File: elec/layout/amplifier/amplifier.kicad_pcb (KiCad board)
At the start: 2 copper layers, 40 x 40 mm, 0 parts

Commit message: building to layout
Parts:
- added C1: , lcsc:C0402, F.Cu at (66.0, 80.6)
- added C10: , lcsc:C0805, F.Cu at (157.2, 103.8)
- added C11: 4.7µF ±10% 16V X5R, lcsc:C0603, F.Cu at (151.0, 60.2)
- added C12: 100nF ±10% 16V X7R, lcsc:C0402, F.Cu at (151.0, 55.2)
- added C13: 22µF ±20% 25V X5R, lcsc:C0805, F.Cu at (170.8, 58.0)
- added C14: , lcsc:C0805, F.Cu at (170.8, 53.0)
- added C15: , lcsc:C0805, F.Cu at (170.8, 48.0)
- added C16: , lcsc:C0402, F.Cu at (170.8, 43.0)
- added C17: , lcsc:C0402, F.Cu at (170.8, 38.0)
- added C18: , lcsc:C0402, F.Cu at (170.8, 33.0)
- added C19: , lcsc:C0402, F.Cu at (156.0, 80.6)
- added C2: 1µF ±10% 25V X5R, lcsc:C0402, F.Cu at (86.0, 80.6)
- added C3: 470nF ±10% 50V X7R, lcsc:C0603, F.Cu at (113.7, 109.1)
- added C4: , lcsc:C0603, F.Cu at (110.9, 111.3)
- added C5: 680nF ±10% 50V X7R, lcsc:C0805, F.Cu at (69.1, 109.7)
- added C6: , lcsc:C0805, F.Cu at (69.1, 104.7)
- added C7: , lcsc:C0603, F.Cu at (116.5, 109.1)
- added C8: , lcsc:C0603, F.Cu at (118.8, 111.4)
- added C9: , lcsc:C0805, F.Cu at (157.2, 108.8)
- added L1: 10µH ±20% 4.5A 68mΩ, lcsc:IND-SMD_L7.3-W6.8, F.Cu at (111.6, 103.3)
- added L2: , lcsc:IND-SMD_L7.3-W6.8, F.Cu at (104.7, 103.3)
- added L3: , lcsc:IND-SMD_L7.3-W6.8, F.Cu at (118.4, 103.3)
- added L4: , lcsc:IND-SMD_L7.3-W6.8, F.Cu at (125.3, 103.3)
- added R1: 10Ω ±1% 62.5mW, lcsc:R0402, F.Cu at (110.7, 116.6)
- added R2: 10kΩ ±1% 62.5mW, lcsc:R0402, F.Cu at (76.0, 80.6)
- added R3: , lcsc:R0402, F.Cu at (96.0, 80.6)
- added R4: , lcsc:R0402, F.Cu at (126.0, 80.6)
- added R5: , lcsc:R0402, F.Cu at (166.0, 80.6)
- added U1: _Texas_Instruments_TAS5825MRHBR, lcsc:VQFN-32_L5.0-W5.0-P0.50-TL-EP, F.Cu at (114.8, 114.6)
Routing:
- net net-10: track 0.00 -> 1.32 mm
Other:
- board outline removed
- board text removed: "{{GITHASH}}"

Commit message: Layout complete
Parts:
- L1: value 10µH ±20% 4.5A 68mΩ -> (none)
- L2: value (none) -> 10µH ±20% 4.5A 68mΩ
- moved C18 103.0 mm to (108.2, 114.8), turned to -90 degrees
- moved C17 92.4 mm to (119.2, 114.7), turned to -90 degrees
- moved C14 90.8 mm to (105.0, 115.6), turned to -90 degrees
- moved C16 87.7 mm to (120.2, 114.7), turned to -90 degrees
- moved C13 86.1 mm to (106.8, 115.6), turned to -90 degrees
- moved C15 83.5 mm to (121.6, 115.4), turned to -90 degrees
- moved C12 72.7 mm to (110.6, 115.7), turned to 90 degrees
- moved C11 69.4 mm to (109.4, 115.8), turned to 90 degrees
- moved R5 64.8 mm to (113.8, 119.0), turned to -90 degrees
- moved C1 64.3 mm to (119.4, 116.4)
- moved C19 60.0 mm to (109.7, 118.8), turned to -90 degrees
- moved R2 52.5 mm to (111.8, 119.0), turned to -90 degrees
- moved C2 49.7 mm to (119.5, 117.4)
- moved R3 41.9 mm to (112.8, 119.0), turned to -90 degrees
- moved C5 39.9 mm to (109.0, 108.8), turned to -90 degrees
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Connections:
- C1 pad 1: net-7 -> net-1
- C1 pad 2: lv -> GND
- C10 pad 2: output_stage_b-net -> GND
- C11 pad 1: hv -> DVDD
- C11 pad 2: lv -> GND
- C12 pad 1: hv -> DVDD
- C12 pad 2: lv -> GND
- C13 pad 1: power_pvdd-net -> PVDD
- C13 pad 2: net -> GND
- C14 pad 1: power_pvdd-net -> PVDD
- C14 pad 2: net -> GND
- C15 pad 1: power_pvdd-net -> PVDD
- C15 pad 2: net -> GND
- C16 pad 1: power_pvdd-net -> PVDD
- C16 pad 2: net -> GND
- C17 pad 1: power_pvdd-net -> PVDD
- C17 pad 2: net -> GND
- C18 pad 1: power_pvdd-net -> PVDD
- C18 pad 2: net -> GND
- C19 pad 1: net-15 -> net-7
- C19 pad 2: net -> GND
- C2 pad 1: net-1 -> net
- C2 pad 2: lv -> GND
- C3 pad 1: net-9 -> net-14
- C3 pad 2: net-8 -> net-12
- C4 pad 1: net-5 -> net-3
- C4 pad 2: net-6 -> net-4
- C5 pad 2: output_stage_a-net -> GND
- C6 pad 1: signal-1 -> signal-3
- C6 pad 2: output_stage_a-net -> GND
- C7 pad 1: net-13 -> net-10
- C7 pad 2: net-14 -> net-8
- C8 pad 1: net-3 -> net-13
- C8 pad 2: net-4 -> net-5
- C9 pad 1: signal-3 -> signal-1
- C9 pad 2: output_stage_b-net -> GND
- L1 pad 1: net-8 -> net-12
- L2 pad 1: net-6 -> net-4
- L2 pad 2: signal-1 -> signal-3
- L3 pad 1: net-14 -> net-8
- L3 pad 2: signal-3 -> signal-1
- L4 pad 1: net-4 -> net-5
- R1 pad 1: net-10 -> net-2
- R1 pad 2: lv -> GND
- R2 pad 1: net-16 -> net-11
- R2 pad 2: hv -> fault-hv
- R3 pad 1: net-12 -> net-9
- R3 pad 2: hv -> mute-hv
- R4 pad 1: net-2 -> net-15
- R4 pad 2: hv -> pdn-hv
- R5 pad 1: net-11 -> net-6
- R5 pad 2: hv -> warn-hv
- U1 pad 1: net-5 -> net-3
- U1 pad 10: net-12 -> net-9
- U1 pad 11: net-11 -> net-6
- U1 pad 17: net-2 -> net-15
- U1 pad 18: net-1 -> net
- U1 pad 19: net-7 -> net-1
- U1 pad 2: net-6 -> net-4
- U1 pad 20: agnd -> GND
- U1 pad 21: amplifier-net-1 -> PVDD
- U1 pad 22: amplifier-net-1 -> PVDD
- U1 pad 23: net-4 -> net-5
- U1 pad 24: net-3 -> net-13
- U1 pad 25: amplifier-net -> GND
- U1 pad 26: amplifier-net -> GND
- U1 pad 27: net-14 -> net-8
- U1 pad 28: net-13 -> net-10
- U1 pad 29: net-9 -> net-14
- U1 pad 3: amplifier-net-1 -> PVDD
- U1 pad 30: net-8 -> net-12
- U1 pad 31: amplifier-net -> GND
- U1 pad 32: amplifier-net -> GND
- U1 pad 33: ep -> GND
- U1 pad 4: amplifier-net-1 -> PVDD
- U1 pad 5: dgnd -> GND
- U1 pad 6: dvdd -> DVDD
- U1 pad 7: net-15 -> net-7
- U1 pad 8: net-10 -> net-2
- U1 pad 9: net-16 -> net-11
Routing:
- net GND: track 0.00 -> 50.8 mm
- net net-5: track 0.00 -> 14.6 mm
- net PVDD: track 0.00 -> 14.5 mm
- net net-4: track 0.00 -> 12.4 mm
- net net-8: track 0.00 -> 10.8 mm
- net net-12: track 0.00 -> 10.2 mm
- net signal-2: track 0.00 -> 8.52 mm
- net signal-3: track 0.00 -> 8.50 mm
- net signal-1: track 0.00 -> 8.48 mm
- net signal: track 0.00 -> 8.47 mm
- net net-7: track 0.00 -> 4.03 mm
- net net-14: track 0.00 -> 3.41 mm
- net DVDD: track 0.00 -> 3.41 mm
- net net-15: track 0.00 -> 3.34 mm
- net net-2: track 0.00 -> 3.34 mm
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- added copper zone on F.Cu, net GND
- added copper zone on F.Cu, net PVDD
- added copper zone on F.Cu, net net-12
- added copper zone on F.Cu, net net-4
- added copper zone on F.Cu, net net-5
- added copper zone on F.Cu, net net-8
- added copper zone on F.Cu, net signal
- added copper zone on F.Cu, net signal-1
- added copper zone on F.Cu, net signal-2
- added copper zone on F.Cu, net signal-3

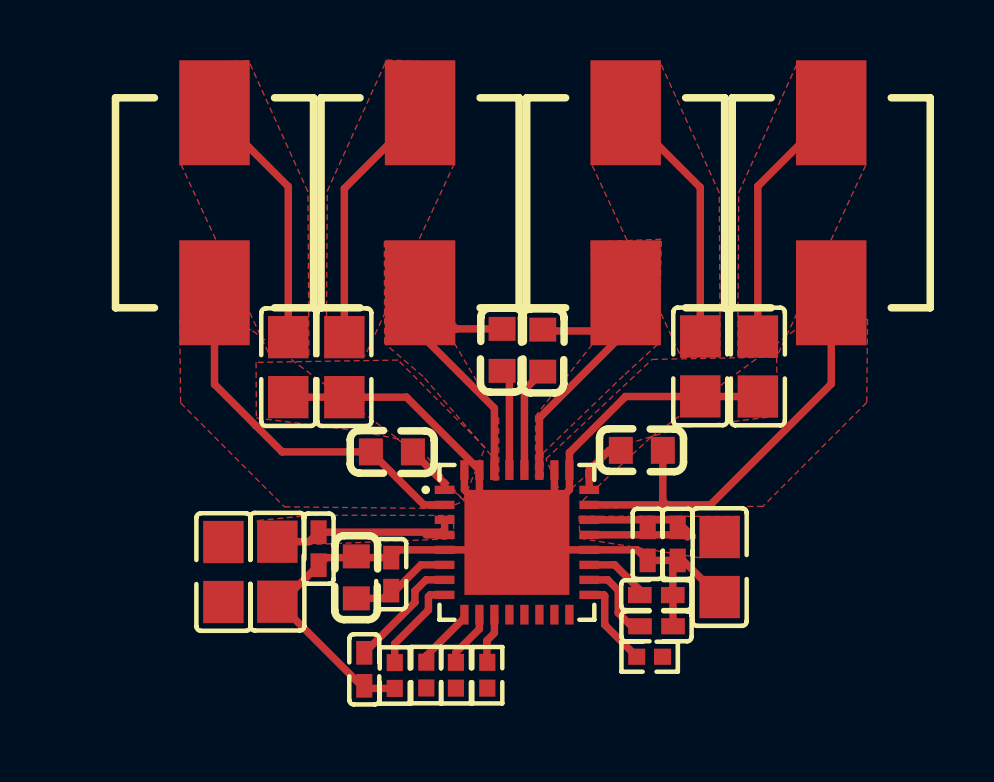
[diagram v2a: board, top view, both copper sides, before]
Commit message: delete unused modules and add library parts
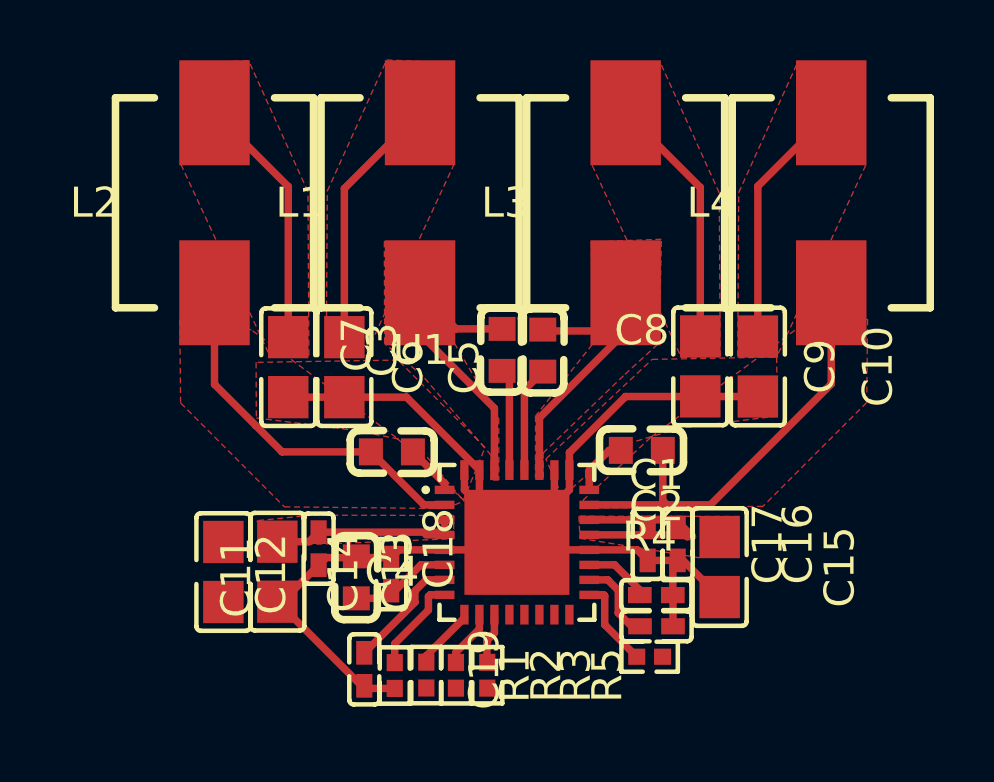
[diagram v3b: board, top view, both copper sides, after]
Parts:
- C1: value (none) -> 1µF ±10% 25V X5R
- C2: value 1µF ±10% 25V X5R -> (none)
- L1: value (none) -> 10µH ±20% 4.5A 68mΩ
- L2: value 10µH ±20% 4.5A 68mΩ -> (none)
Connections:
- C1 pad 1: net-1 -> net-14
- C1 pad 2: GND -> net-1
- C10 pad 2: GND -> net-1
- C11 pad 2: GND -> net-1
- C12 pad 2: GND -> net-1
- C13 pad 2: GND -> net-1
- C14 pad 2: GND -> net-1
- C15 pad 2: GND -> net-1
- C16 pad 2: GND -> net-1
- C17 pad 2: GND -> net-1
- C18 pad 2: GND -> net-1
- C19 pad 1: net-7 -> net-8
- C19 pad 2: GND -> net-1
- C2 pad 1: net -> net-15
- C2 pad 2: GND -> net-1
- C3 pad 1: net-14 -> net-16
- C3 pad 2: net-12 -> net-4
- C4 pad 1: net-3 -> net-2
- C4 pad 2: net-4 -> net-3
- C5 pad 1: signal-2 -> signal-1
- C5 pad 2: GND -> net-1
- C6 pad 1: signal-3 -> signal-2
- C6 pad 2: GND -> net-1
- C7 pad 1: net-10 -> net-5
- C7 pad 2: net-8 -> net-6
- C8 pad 1: net-13 -> net-10
- C8 pad 2: net-5 -> net
- C9 pad 1: signal-1 -> signal-3
- C9 pad 2: GND -> net-1
- L1 pad 1: net-12 -> net-4
- L1 pad 2: signal-2 -> signal-1
- L2 pad 1: net-4 -> net-3
- L2 pad 2: signal-3 -> signal-2
- L3 pad 1: net-8 -> net-6
- L3 pad 2: signal-1 -> signal-3
- L4 pad 1: net-5 -> net
- R1 pad 1: net-2 -> net-9
- R1 pad 2: GND -> net-1
- R2 pad 1: net-11 -> net-7
- R3 pad 1: net-9 -> net-11
- R4 pad 1: net-15 -> net-13
- R5 pad 1: net-6 -> net-12
- U1 pad 1: net-3 -> net-2
- U1 pad 10: net-9 -> net-11
- U1 pad 11: net-6 -> net-12
- U1 pad 17: net-15 -> net-13
- U1 pad 18: net -> net-15
- U1 pad 19: net-1 -> net-14
- U1 pad 2: net-4 -> net-3
- U1 pad 20: GND -> net-1
- U1 pad 23: net-5 -> net
- U1 pad 24: net-13 -> net-10
- U1 pad 25: GND -> net-1
- U1 pad 26: GND -> net-1
- U1 pad 27: net-8 -> net-6
- U1 pad 28: net-10 -> net-5
- U1 pad 29: net-14 -> net-16
- U1 pad 30: net-12 -> net-4
- U1 pad 31: GND -> net-1
- U1 pad 32: GND -> net-1
- U1 pad 33: GND -> net-1
- U1 pad 5: GND -> net-1
- U1 pad 7: net-7 -> net-8
- U1 pad 8: net-2 -> net-9
- U1 pad 9: net-11 -> net-7
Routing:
- net GND: track 50.8 -> 0.00 mm
- net (no net): track 0.00 -> 50.8 mm
- added copper zone on F.Cu, net (none)
- removed copper zone on F.Cu, net GND

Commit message: import copper features to hat board
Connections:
- C1 pad 1: net-14 -> net-12
- C1 pad 2: net-1 -> net-2
- C10 pad 1: signal -> signal-3
- C10 pad 2: net-1 -> net-2
- C11 pad 2: net-1 -> net-2
- C12 pad 2: net-1 -> net-2
- C13 pad 2: net-1 -> net-2
- C14 pad 2: net-1 -> net-2
- C15 pad 2: net-1 -> net-2
- C16 pad 2: net-1 -> net-2
- C17 pad 2: net-1 -> net-2
- C18 pad 2: net-1 -> net-2
- C19 pad 1: net-8 -> net-5
- C19 pad 2: net-1 -> net-2
- C2 pad 1: net-15 -> net-16
- C2 pad 2: net-1 -> net-2
- C3 pad 1: net-16 -> net-13
- C3 pad 2: net-4 -> net-14
- C4 pad 1: net-2 -> net-7
- C4 pad 2: net-3 -> net-8
- C5 pad 1: signal-1 -> signal
- C5 pad 2: net-1 -> net-2
- C6 pad 1: signal-2 -> signal-1
- C6 pad 2: net-1 -> net-2
- C7 pad 1: net-5 -> net
- C7 pad 2: net-6 -> net-1
- C8 pad 1: net-10 -> net-4
- C8 pad 2: net -> net-3
- C9 pad 1: signal-3 -> signal-2
- C9 pad 2: net-1 -> net-2
- L1 pad 1: net-4 -> net-14
- L1 pad 2: signal-1 -> signal
- L2 pad 1: net-3 -> net-8
- L2 pad 2: signal-2 -> signal-1
- L3 pad 1: net-6 -> net-1
- L3 pad 2: signal-3 -> signal-2
- L4 pad 1: net -> net-3
- L4 pad 2: signal -> signal-3
- R1 pad 1: net-9 -> net-10
- R1 pad 2: net-1 -> net-2
- R2 pad 1: net-7 -> net-6
- R4 pad 1: net-13 -> net-9
- R5 pad 1: net-12 -> net-15
- U1 pad 1: net-2 -> net-7
- U1 pad 11: net-12 -> net-15
- U1 pad 17: net-13 -> net-9
- U1 pad 18: net-15 -> net-16
- U1 pad 19: net-14 -> net-12
- U1 pad 2: net-3 -> net-8
- U1 pad 20: net-1 -> net-2
- U1 pad 23: net -> net-3
- U1 pad 24: net-10 -> net-4
- U1 pad 25: net-1 -> net-2
- U1 pad 26: net-1 -> net-2
- U1 pad 27: net-6 -> net-1
- U1 pad 28: net-5 -> net
- U1 pad 29: net-16 -> net-13
- U1 pad 30: net-4 -> net-14
- U1 pad 31: net-1 -> net-2
- U1 pad 32: net-1 -> net-2
- U1 pad 33: net-1 -> net-2
- U1 pad 5: net-1 -> net-2
- U1 pad 7: net-8 -> net-5
- U1 pad 8: net-9 -> net-10
- U1 pad 9: net-7 -> net-6

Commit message: builds working
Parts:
- C10, C6, C9: value (none) -> 680nF ±10% 50V X7R
- C14, C15: value (none) -> 22µF ±20% 25V X5R
- C16, C17, C18: value (none) -> 100nF ±10% 16V X7R
- C19, C2: value (none) -> 1µF ±10% 25V X5R
- C4, C7, C8: value (none) -> 470nF ±10% 50V X7R
- L2, L3, L4: value (none) -> 10µH ±20% 4.5A 68mΩ
- R3, R4, R5: value (none) -> 10kΩ ±1% 62.5mW
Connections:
- net DVDD renamed hv
- C1 pad 1: net-12 -> net-6
- C1 pad 2: net-2 -> net
- C10 pad 1: signal-3 -> signal-1
- C10 pad 2: net-2 -> net
- C11 pad 2: net-2 -> net
- C12 pad 2: net-2 -> net
- C13 pad 1: PVDD -> net-4
- C13 pad 2: net-2 -> net
- C14 pad 1: PVDD -> net-4
- C14 pad 2: net-2 -> net
- C15 pad 1: PVDD -> net-4
- C15 pad 2: net-2 -> net
- C16 pad 1: PVDD -> net-4
- C16 pad 2: net-2 -> net
- C17 pad 1: PVDD -> net-4
- C17 pad 2: net-2 -> net
- C18 pad 1: PVDD -> net-4
- C18 pad 2: net-2 -> net
- C19 pad 1: net-5 -> net-12
- C19 pad 2: net-2 -> net
- C2 pad 1: net-16 -> net-5
- C2 pad 2: net-2 -> net
- C3 pad 1: net-13 -> net-10
- C3 pad 2: net-14 -> net-8
- C4 pad 1: net-7 -> net-13
- C4 pad 2: net-8 -> net-14
- C5 pad 2: net-2 -> net
- C6 pad 1: signal-1 -> signal-2
- C6 pad 2: net-2 -> net
- C7 pad 1: net -> net-1
- C7 pad 2: net-1 -> net-2
- C8 pad 1: net-4 -> net-11
- C8 pad 2: net-3 -> net-7
- C9 pad 1: signal-2 -> signal-3
- C9 pad 2: net-2 -> net
- L1 pad 1: net-14 -> net-8
- L2 pad 1: net-8 -> net-14
- L2 pad 2: signal-1 -> signal-2
- L3 pad 1: net-1 -> net-2
- L3 pad 2: signal-2 -> signal-3
- L4 pad 1: net-3 -> net-7
- L4 pad 2: signal-3 -> signal-1
- R1 pad 1: net-10 -> net-3
- R1 pad 2: net-2 -> net
- R2 pad 1: net-6 -> net-15
- R3 pad 1: net-11 -> net-16
- R4 pad 1: net-9 -> net-17
- R5 pad 1: net-15 -> net-9
- U1 pad 1: net-7 -> net-13
- U1 pad 10: net-11 -> net-16
- U1 pad 11: net-15 -> net-9
- U1 pad 17: net-9 -> net-17
- U1 pad 18: net-16 -> net-5
- U1 pad 19: net-12 -> net-6
- U1 pad 2: net-8 -> net-14
- U1 pad 20: net-2 -> net
- U1 pad 21: PVDD -> net-4
- U1 pad 22: PVDD -> net-4
- U1 pad 23: net-3 -> net-7
- U1 pad 24: net-4 -> net-11
- U1 pad 25: net-2 -> net
- U1 pad 26: net-2 -> net
- U1 pad 27: net-1 -> net-2
- U1 pad 28: net -> net-1
- U1 pad 29: net-13 -> net-10
- U1 pad 3: PVDD -> net-4
- U1 pad 30: net-14 -> net-8
- U1 pad 31: net-2 -> net
- U1 pad 32: net-2 -> net
- U1 pad 33: net-2 -> net
- U1 pad 4: PVDD -> net-4
- U1 pad 5: net-2 -> net
- U1 pad 7: net-5 -> net-12
- U1 pad 8: net-10 -> net-3
- U1 pad 9: net-6 -> net-15
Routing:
- net (no net): track 50.8 -> 65.3 mm
- net PVDD: track 14.5 -> 0.00 mm
- removed copper zone on F.Cu, net PVDD

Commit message: Build full
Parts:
- C1, C19, C2: value 1µF ±10% 25V X5R -> 1µF ±10% 10V X5R
- C11: value 4.7µF ±10% 16V X5R -> 100nF ±10% 50V X7R
- C12, C16, C17, C18: value 100nF ±10% 16V X7R -> 100nF ±10% 50V X7R; footprint lcsc:C0402 -> lcsc:C0603
- C13, C14, C15: value 22µF ±20% 25V X5R -> 100nF ±10% 50V X7R; footprint lcsc:C0805 -> lcsc:C0603
- C3, C4, C7, C8: footprint lcsc:C0603 -> lcsc:CAP-SMD_L1.6-W0.8-3
- L1, L2, L3, L4: value 10µH ±20% 4.5A 68mΩ -> 10µH ±20% infHz 4.5A 68mΩ
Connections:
- net fault-hv renamed hv-3
- net mute-hv renamed hv-1
- net pdn-hv renamed hv-4
- C1 pad 1: net-6 -> net-10
- C1 pad 2: net -> net-4
- C10 pad 1: signal-1 -> signal-2
- C10 pad 2: net -> net-4
- C11 pad 1: hv -> hv-2
- C11 pad 2: net -> net-4
- C12 pad 1: hv -> hv-2
- C12 pad 2: net -> net-4
- C13 pad 1: net-4 -> net-5
- C13 pad 2: net -> net-4
- C14 pad 1: net-4 -> net-5
- C14 pad 2: net -> net-4
- C15 pad 1: net-4 -> net-5
- C15 pad 2: net -> net-4
- C16 pad 1: net-4 -> net-5
- C16 pad 2: net -> net-4
- C17 pad 1: net-4 -> net-5
- C17 pad 2: net -> net-4
- C18 pad 1: net-4 -> net-5
- C18 pad 2: net -> net-4
- C19 pad 1: net-12 -> net-11
- C19 pad 2: net -> net-4
- C2 pad 1: net-5 -> net-3
- C2 pad 2: net -> net-4
- C3 pad 1: net-10 -> net-14
- C3 pad 2: net-8 -> net-9
- C4 pad 1: net-13 -> net-7
- C4 pad 2: net-14 -> net-8
- C5 pad 1: signal -> signal-1
- C5 pad 2: net -> net-4
- C6 pad 1: signal-2 -> signal-3
- C6 pad 2: net -> net-4
- C7 pad 1: net-1 -> net
- C7 pad 2: net-2 -> net-1
- C8 pad 1: net-11 -> net-16
- C8 pad 2: net-7 -> net-13
- C9 pad 1: signal-3 -> signal
- C9 pad 2: net -> net-4
- L1 pad 1: net-8 -> net-9
- L1 pad 2: signal -> signal-1
- L2 pad 1: net-14 -> net-8
- L2 pad 2: signal-2 -> signal-3
- L3 pad 1: net-2 -> net-1
- L3 pad 2: signal-3 -> signal
- L4 pad 1: net-7 -> net-13
- L4 pad 2: signal-1 -> signal-2
- R1 pad 1: net-3 -> net-12
- R1 pad 2: net -> net-4
- R2 pad 1: net-15 -> net-17
- R3 pad 1: net-16 -> net-6
- R4 pad 1: net-17 -> net-15
- R5 pad 1: net-9 -> net-2
- R5 pad 2: warn-hv -> hv
- U1 pad 1: net-13 -> net-7
- U1 pad 10: net-16 -> net-6
- U1 pad 11: net-9 -> net-2
- U1 pad 17: net-17 -> net-15
- U1 pad 18: net-5 -> net-3
- U1 pad 19: net-6 -> net-10
- U1 pad 2: net-14 -> net-8
- U1 pad 20: net -> net-4
- U1 pad 21: net-4 -> net-5
- U1 pad 22: net-4 -> net-5
- U1 pad 23: net-7 -> net-13
- U1 pad 24: net-11 -> net-16
- U1 pad 25: net -> net-4
- U1 pad 26: net -> net-4
- U1 pad 27: net-2 -> net-1
- U1 pad 28: net-1 -> net
- U1 pad 29: net-10 -> net-14
- U1 pad 3: net-4 -> net-5
- U1 pad 30: net-8 -> net-9
- U1 pad 31: net -> net-4
- U1 pad 32: net -> net-4
- U1 pad 33: net -> net-4
- U1 pad 4: net-4 -> net-5
- U1 pad 5: net -> net-4
- U1 pad 6: hv -> hv-2
- U1 pad 7: net-12 -> net-11
- U1 pad 8: net-3 -> net-12
- U1 pad 9: net-15 -> net-17
